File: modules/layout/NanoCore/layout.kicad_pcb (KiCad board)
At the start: 4 copper layers, 19 x 44 mm, 36 parts, among them IC1 ATMEGA328PMAU, IC2 AMS1117M5_0, IC3 FT231XQMR, J1 2.54mm 15x1, J2 2.54mm 15x1, J3 10033526MN3212LF, J4 2.54mm 3x2, Y1 16MHz 18pF

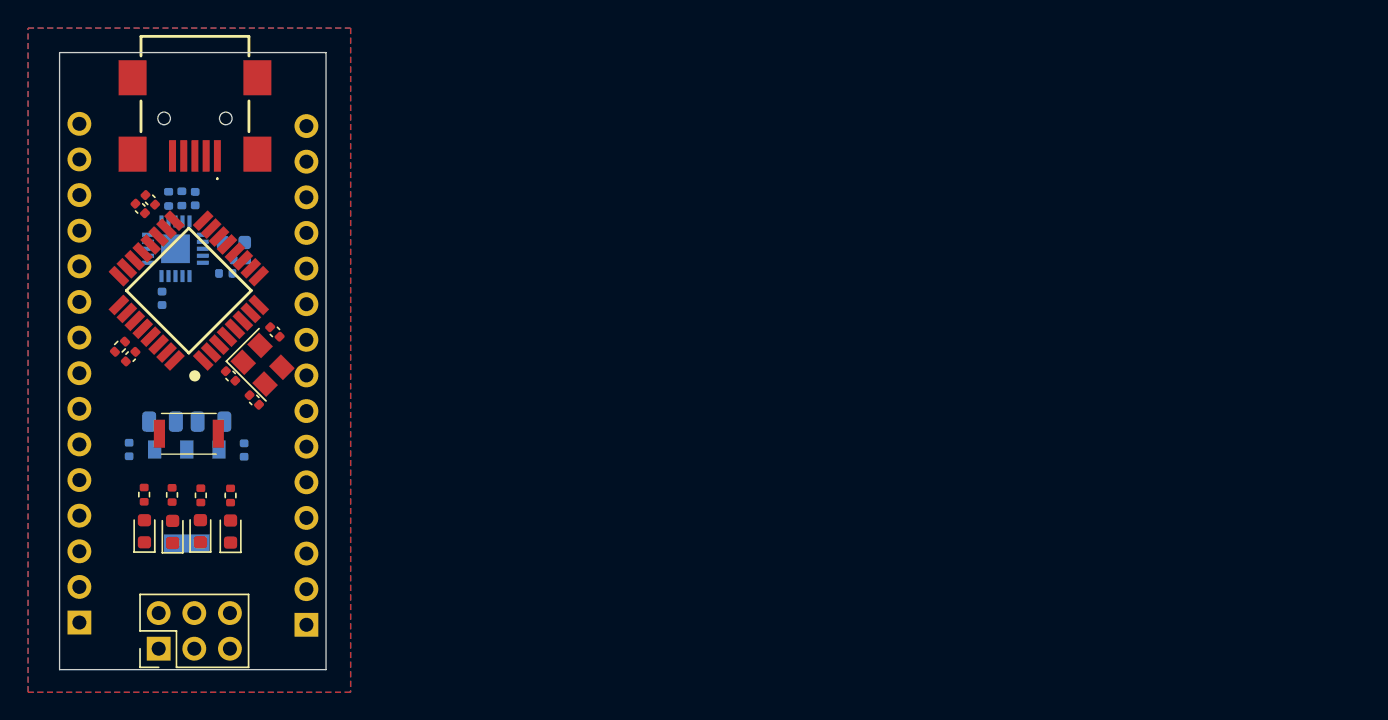
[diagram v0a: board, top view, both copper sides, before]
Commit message: use carrier and core arch
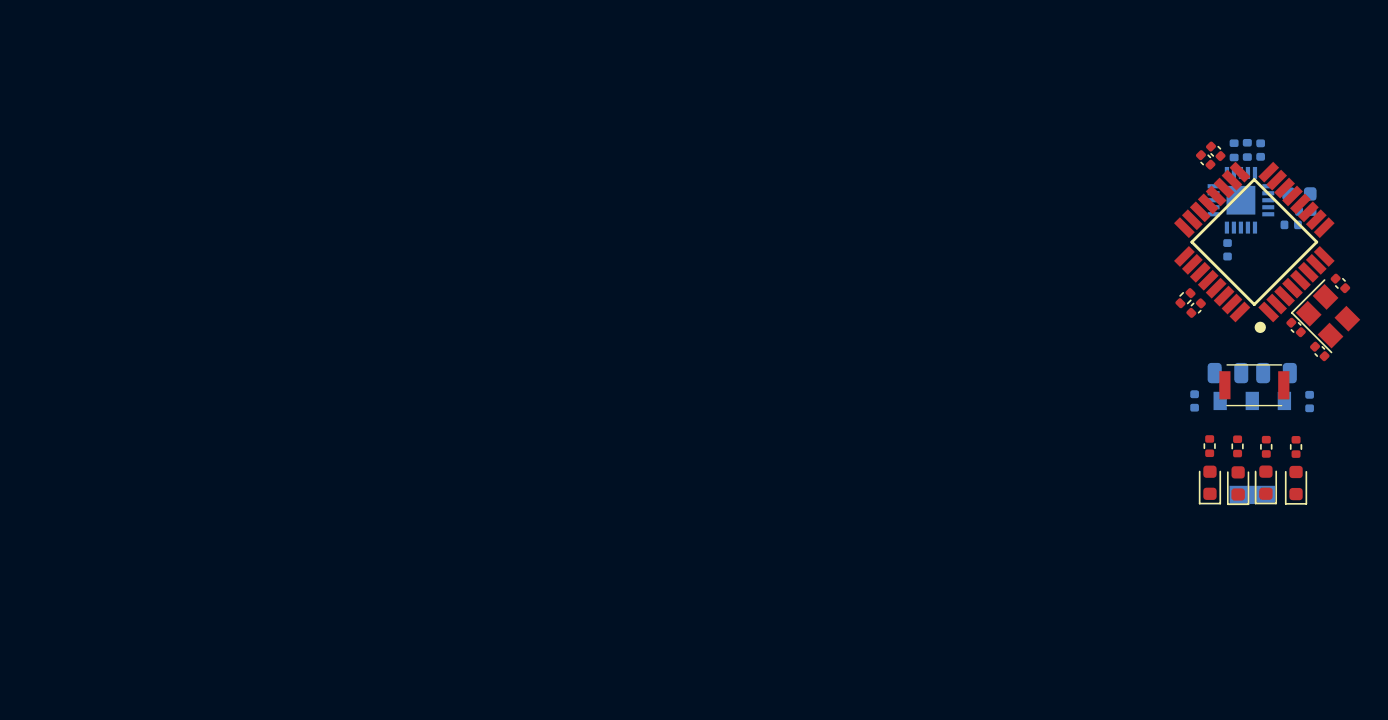
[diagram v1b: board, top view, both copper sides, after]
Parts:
- removed J1, J2: 2.54mm 15x1, PinHeader_1x15_P2.54mm_Vertical:PinHeader_1x15_P2.54mm_Vertical
- removed J3: 10033526MN3212LF, 10033526N3212LF:10033526N3212LF
- removed J4: 2.54mm 3x2, PinHeader_2x03_P2.54mm_Vertical:PinHeader_2x03_P2.54mm_Vertical
- removed V1: ?, version-footprint:version-footprint
- moved C11 76.1 mm to (147.8, 87.7)
- moved C14 76.1 mm to (151.0, 92.1)
- moved D3 76.1 mm to (148.1, 111.4)
- moved IC2 76.1 mm to (147.2, 109.0)
- moved IC3 76.1 mm to (146.4, 91.3)
- moved R4 76.1 mm to (148.2, 108.9)
- moved C1 76.1 mm to (143.2, 99.0)
- moved C10 76.1 mm to (143.1, 105.6)
- moved C12 76.1 mm to (145.4, 94.8)
- moved C13 76.1 mm to (149.9, 93.1)
- moved C15 76.1 mm to (150.5, 90.9)
- moved C2 76.1 mm to (143.9, 88.4)
- moved C3 76.1 mm to (144.6, 87.8)
- moved C4 76.1 mm to (150.3, 100.4)
- moved C5 76.1 mm to (152.0, 102.1)
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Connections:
- net NANO.DTR renamed DTR
- net NANO.LED_L_ANODE renamed LED_L_ANODE
- net NANO.LED_PWR_ANODE renamed LED_PWR_ANODE
- net NANO.MCU.oscpair_XIN renamed MCU.oscpair_XIN
- net NANO.MCU.oscpair_XOUT renamed MCU.oscpair_XOUT
- net NANO.USB_SERIAL.CBUS0 renamed USB_SERIAL.CBUS0
- net NANO.USB_SERIAL.CBUS1 renamed USB_SERIAL.CBUS1
- net NANO.USB_SERIAL.CBUS2 renamed USB_SERIAL.CBUS2
- net NANO.USB_SERIAL.CBUS3 renamed USB_SERIAL.CBUS3
- net NANO.USB_SERIAL.CTS renamed USB_SERIAL.CTS
- net NANO.USB_SERIAL.NC renamed USB_SERIAL.NC
- net NANO.USB_SERIAL.NC_2 renamed USB_SERIAL.NC_2
- net NANO.USB_SERIAL.NC_3 renamed USB_SERIAL.NC_3
- net NANO.USB_SERIAL.P3V3OUT renamed USB_SERIAL.P3V3OUT
- net NANO.USB_SERIAL.RTS renamed USB_SERIAL.RTS
- net NANO.USB_SERIAL.RX_LED_ANODE renamed USB_SERIAL.RX_LED_ANODE
- net NANO.USB_SERIAL.TX_LED_ANODE renamed USB_SERIAL.TX_LED_ANODE
- net NANO.USB_SERIAL.USBDM_INTERNAL renamed USB_SERIAL.USBDM_INTERNAL
- net NANO.USB_SERIAL.USBDP_INTERNAL renamed USB_SERIAL.USBDP_INTERNAL
- C1 pad 2: NANO.RESET -> RESET
- C10 pad 1: NANO.VCC_5V -> VCC_5V
- C12 pad 1: NANO.VCC_5V -> VCC_5V
- C13 pad 1: NANO.VCC_5V -> VCC_5V
- C14 pad 1: NANO.VCC_5V -> VCC_5V
- C15 pad 1: NANO.VCC_5V -> VCC_5V
- C2 pad 1: NANO.VCC_5V -> VCC_5V
- C3 pad 1: NANO.VCC_5V -> VCC_5V
- C4 pad 1: NANO.VCC_5V -> VCC_5V
- C7 pad 1: VCC_VIN -> USB_VBUS
- C8 pad 1: VCC_VIN -> USB_VBUS
- C9 pad 1: NANO.VCC_5V -> VCC_5V
- IC1 pad 18: NANO.VCC_5V -> VCC_5V
- IC1 pad 20: NANO.AREF -> AREF
- IC1 pad 29: NANO.RESET -> RESET
- IC1 pad 4: NANO.VCC_5V -> VCC_5V
- IC1 pad 6: NANO.VCC_5V -> VCC_5V
- IC2 pad 2: NANO.VCC_5V -> VCC_5V
- IC2 pad 3: VCC_VIN -> USB_VBUS
- IC3 pad 11: NANO.VCC_5V -> VCC_5V
- IC3 pad 12: NANO.VCC_5V -> VCC_5V
- IC3 pad 20: NANO.VCC_5V -> VCC_5V
- R1 pad 1: NANO.RESET -> RESET
- R1 pad 2: NANO.VCC_5V -> VCC_5V
- R3 pad 1: NANO.VCC_5V -> VCC_5V
- R4 pad 1: NANO.VCC_5V -> VCC_5V
- R5 pad 1: NANO.VCC_5V -> VCC_5V
- R6 pad 2: NANO.USB_D_N -> USB_DATA_D_N
- R7 pad 2: NANO.USB_D_P -> USB_DATA_D_P
- S1 pad 1: NANO.RESET -> RESET
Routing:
- removed copper zone on B.Cu, net GND
- removed copper zone on F.Cu, net GND
- removed copper zone on In1.Cu, net GND
- removed copper zone on In2.Cu, net VCC_5V
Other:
- board outline removed
- board text removed: "0"
- board text removed: "0 mm"
- board text removed: "0.01 mm"
- board text removed: "0.0152 mm"
- board text removed: "0.025"
- board text removed: "0.035 mm"
- board text removed: "0.0900 mm / 0.0900 mm"
- board text removed: "0.1500 mm"
- board text removed: "0.2104 mm"
- board text removed: "1"
- board text removed: "1.065 mm"
- board text removed: "1.6062 mm"
- board text removed: "19.0000 mm x 44.0000 mm"
- board text removed: "3.3"
- board text removed: "4"
- board text removed: "4.4"
- board text removed: "4.6"
- board text removed: "B.Cu"
- board text removed: "B.Mask"
- board text removed: "B.Paste"
- board text removed: "B.Silkscreen"
- board text removed: "BOARD CHARACTERISTICS"
- board text removed: "Blue"
- board text removed: "Board Thickness:"
- board text removed: "Board overall dimensions:"
- board text removed: "Bottom Silk Screen"
- board text removed: "Bottom Solder Mask"
- board text removed: "Bottom Solder Paste"
- board text removed: "Castellated pads:"
- board text removed: "Color"
- board text removed: "Copper Finish:"
- board text removed: "Copper Layer Count:"
- board text removed: "Dielectric"
- board text removed: "ENIG"
- board text removed: "Edge card connectors:"
- board text removed: "Epsilon R"
- board text removed: "F.Cu"
- board text removed: "F.Mask"
- board text removed: "F.Paste"
- board text removed: "F.Silkscreen"
- board text removed: "FR4-Core"
- board text removed: "Impedance Control:"
- board text removed: "In1.Cu"
- board text removed: "In2.Cu"
- board text removed: "Layer Name"
- board text removed: "Loss Tangent"
- board text removed: "Material"
- board text removed: "Min hole diameter:"
- board text removed: "Min track/spacing:"
- board text removed: "No"
- board text removed: "Not specified"
- board text removed: "Plated Board Edge:"
- board text removed: "Prepreg"
- board text removed: "Thickness (mm)"
- board text removed: "Top Silk Screen"
- board text removed: "Top Solder Mask"
- board text removed: "Top Solder Paste"
- board text removed: "Type"
- board text removed: "White"
- board text removed: "copper"
- board text removed: "core"
- board text removed: "prepreg"
